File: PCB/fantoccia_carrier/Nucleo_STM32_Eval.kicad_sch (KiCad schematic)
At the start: 2 parts, among them J1 BU2450SM-JJ-GTR, U1 NUCLEO144-H743ZI

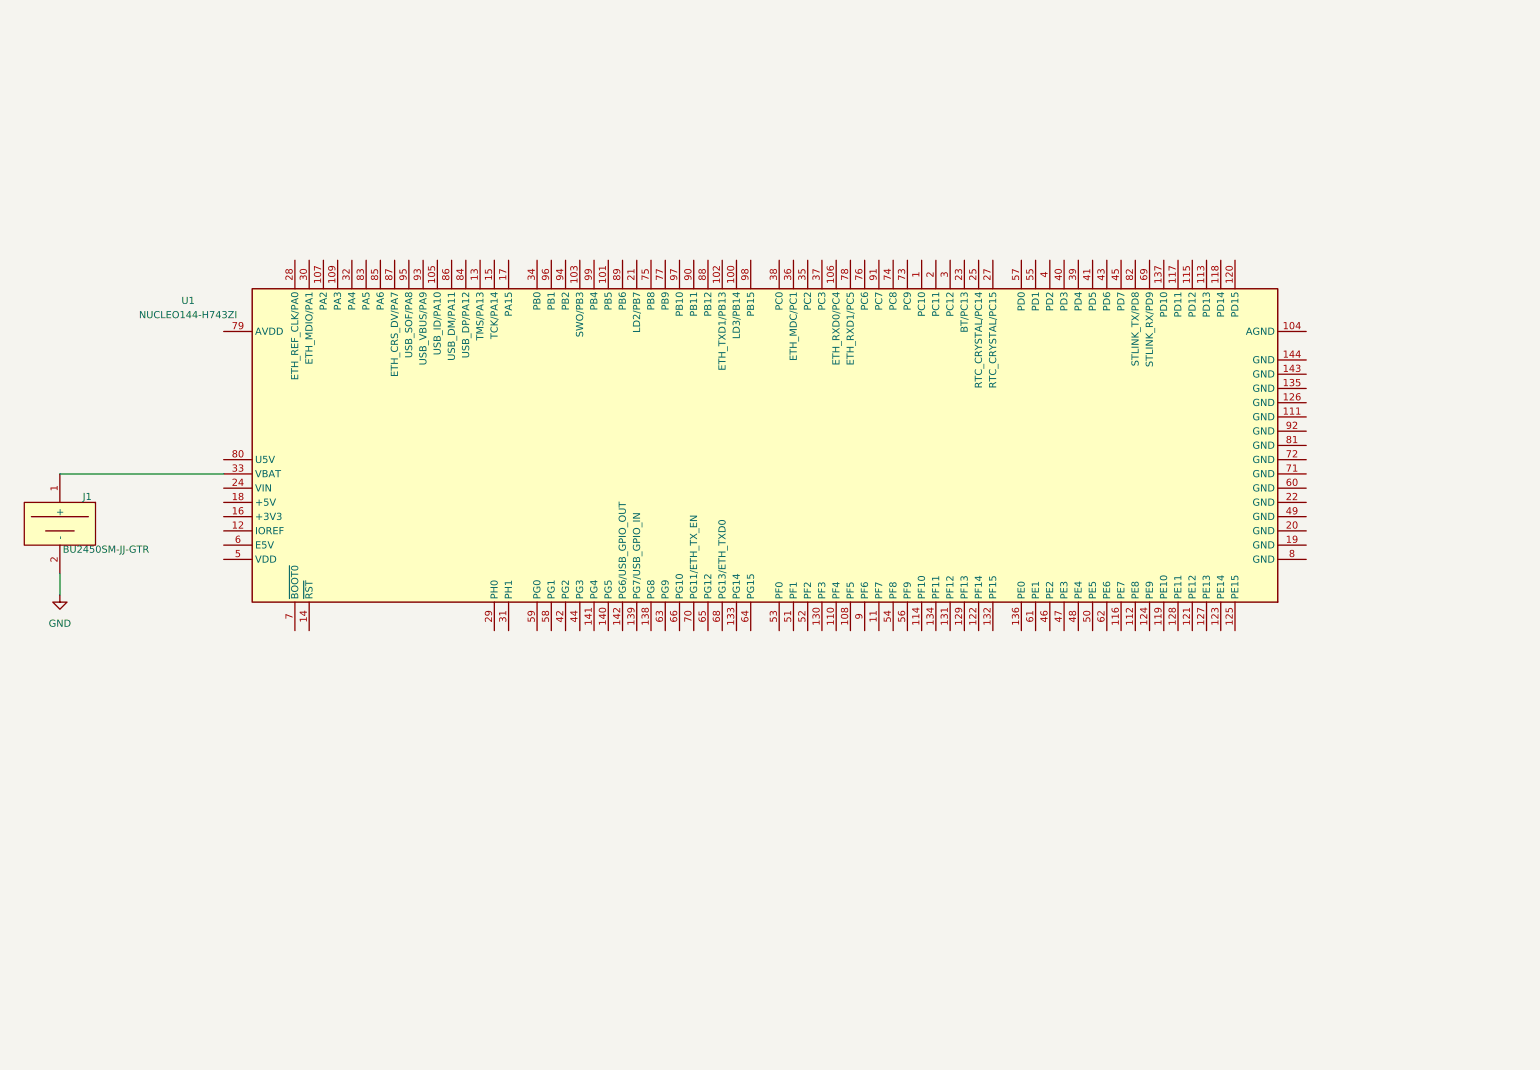
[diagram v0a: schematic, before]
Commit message: PCB Created
Schematic mostly finished, just need to figure out pinning and add more TVS protection. Created PCB might need to tweak footprint.
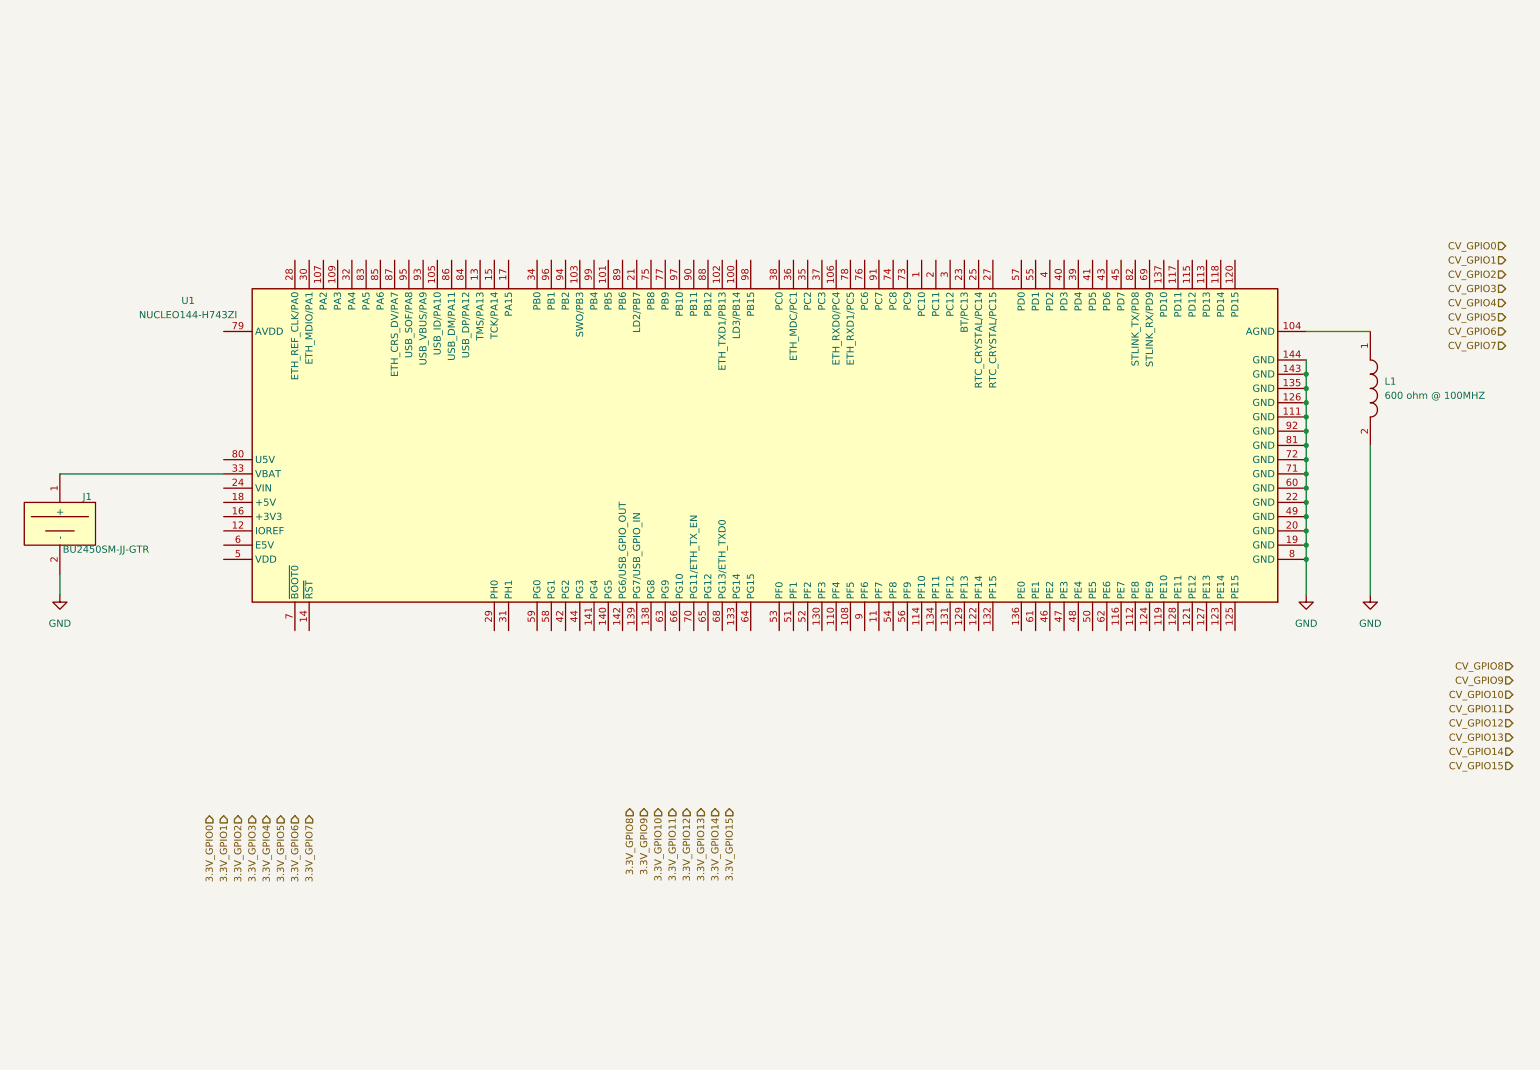
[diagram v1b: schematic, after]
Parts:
- added L1: HZ0805E601R-10, AVR-KiCAD-Lib-Inductors:HZ0805E601R-10, symbol AVR-KiCAD-Lib-Inductors:HZ0805E601R-10
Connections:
- net GND: now also U1.111 (GND), U1.126 (GND), U1.135 (GND), U1.143 (GND), U1.144 (GND), U1.19 (GND), U1.20 (GND), U1.22 (GND), U1.49 (GND), U1.60 (GND), U1.71 (GND), U1.72 (GND), U1.8 (GND), U1.81 (GND), U1.92 (GND), L1.2
- net at U1.104 (AGND): now also L1.1

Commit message: PCB progress and feature updates
Added another bank of 5V channels. PCB layout figured out, board shape defined. 3D model added to STM32 evaluation kit. Now just need to determine pinout and add protection circuitry to pins.
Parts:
- added D1, D2, D3, D4: LTST-C194TBKT, AVR-KiCAD-Lib-Diodes:LED0603, symbol AVR-KiCAD-Lib-Diodes:LTST-C194TBKT
- added R1, R2, R3, R4: RC0603FR-072K2L, AVR-KiCAD-Lib-Resistors:R0603, symbol AVR-KiCAD-Lib-Resistors:RC0603FR-072K2L
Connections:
- net GND: now also D1.2, D2.2, D3.2, D4.2
- new net: D4.1, R4.2
- new net: D1.1, R1.2
- new net: D3.1, R3.2
- new net: D2.1, R2.2

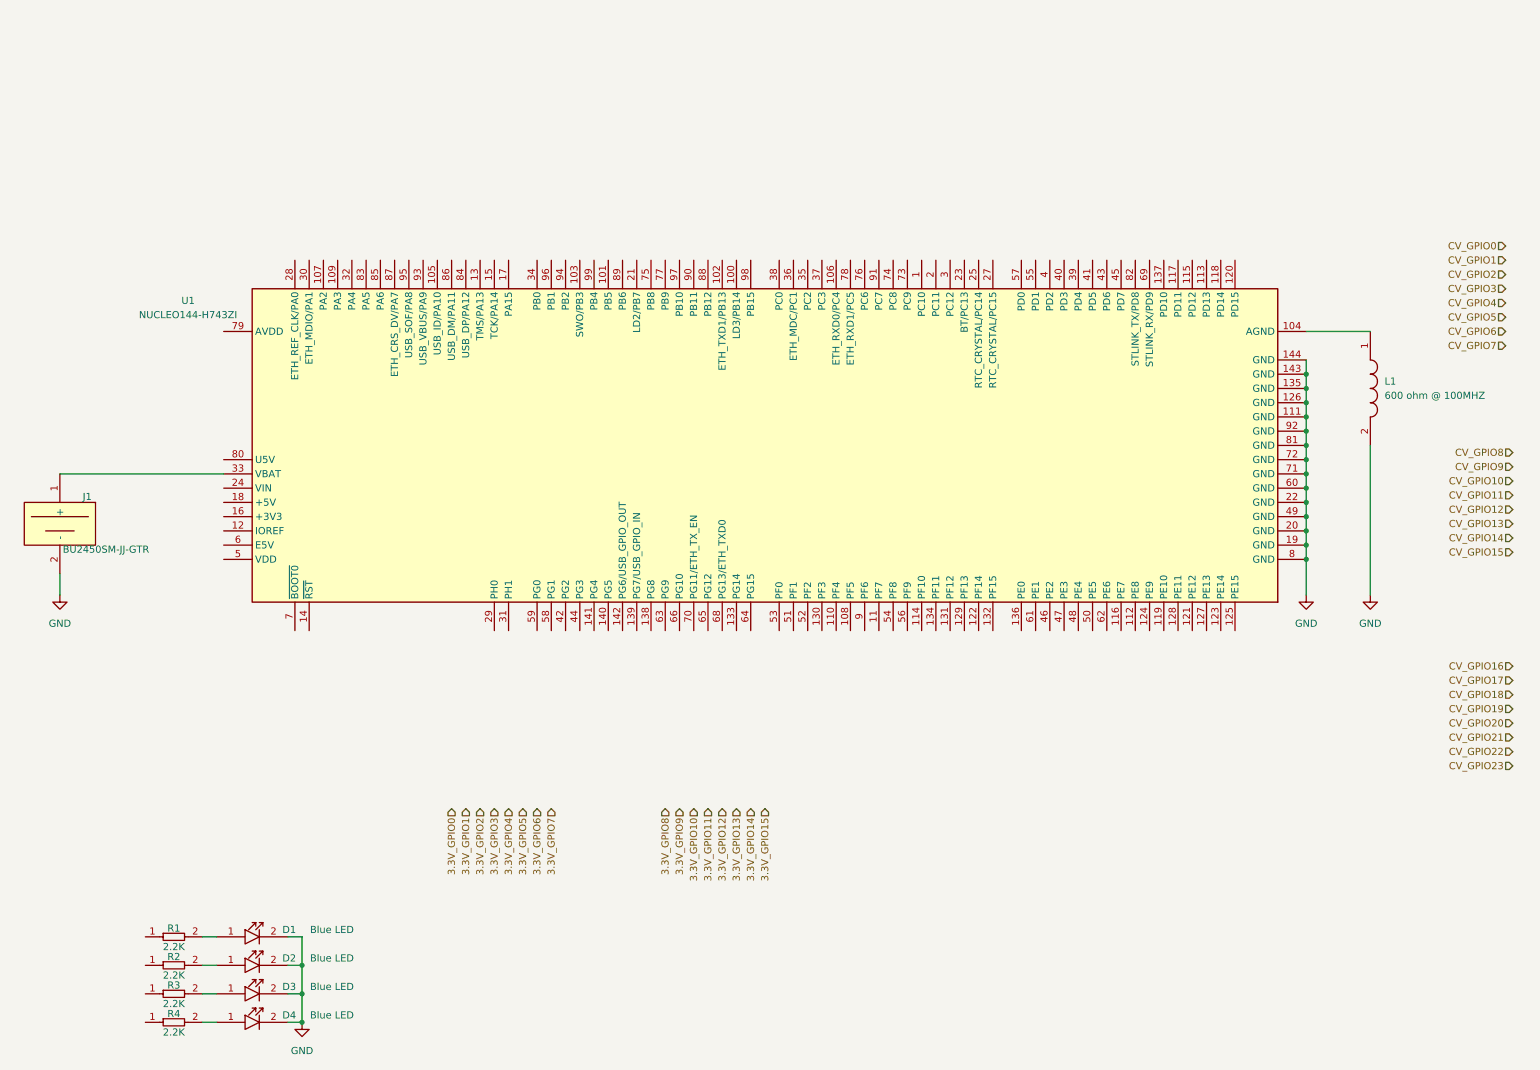
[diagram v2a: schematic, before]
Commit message: Design Rules
Created Design rules, added more IO connections, need to figure out pinning next.
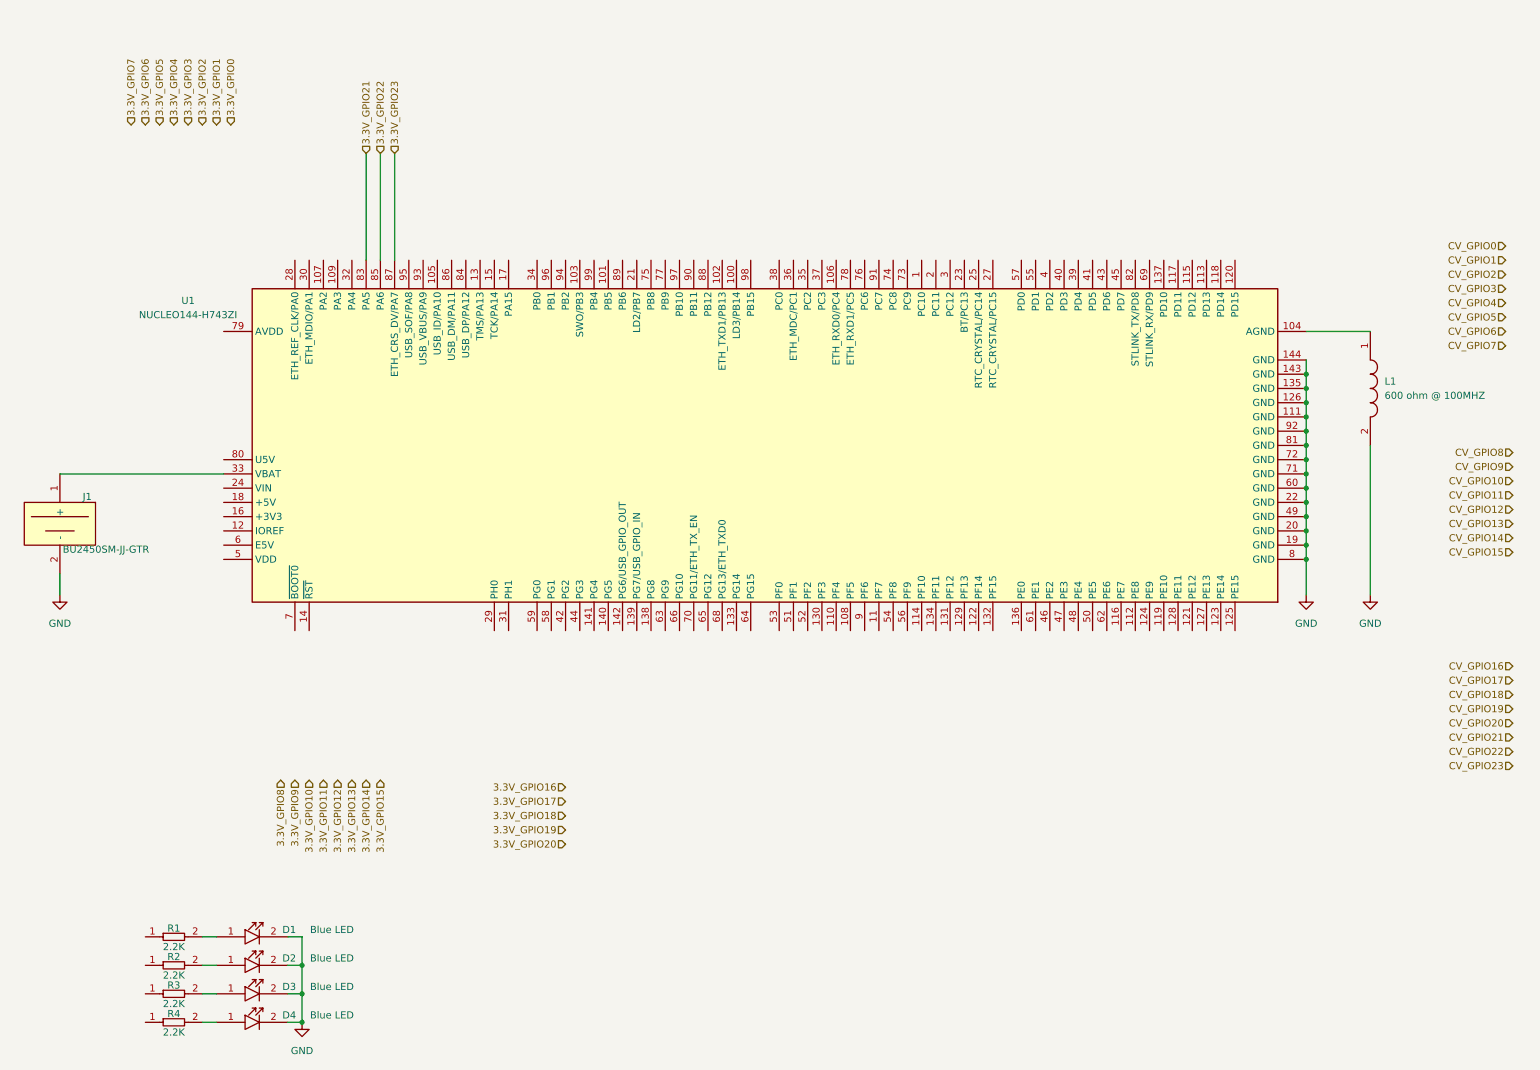
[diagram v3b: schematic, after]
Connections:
- net 3.3V_GPIO21: now reaches U1.83 (PA5)
- net 3.3V_GPIO22: now reaches U1.85 (PA6)
- net 3.3V_GPIO23: now reaches U1.87 (ETH_CRS_DV/PA7)
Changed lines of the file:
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@@
+	(wire
+		(pts
+			(xy 74.93 35.56) (xy 74.93 54.61)
+		)
+		(stroke
+			(width 0)
+			(type default)
+		)
+	)
 	(wire
 		(pts
@@
 	(wire
 		(pts
+			(xy 77.47 35.56) (xy 77.47 54.61)
+		)
+		(stroke
+			(width 0)
+			(type default)
+		)
+	)
+	(wire
+		(pts
+			(xy 80.01 35.56) (xy 80.01 54.61)
+		)
+		(stroke
+			(width 0)
+			(type default)
+		)
+	)
+	(wire
+		(pts
 			(xy 242.57 80.01) (xy 242.57 82.55)
 		)
@@
 	(hierarchical_label "3.3V_GPIO3"
 		(shape input)
-		(at 97.79 152.4 270)
-		(fields_autoplaced yes)
-		(effects
-			(font
-				(size 1.27 1.27)
-			)
-			(justify right)
+		(at 43.18 30.48 90)
+		(fields_autoplaced yes)
+		(effects
+			(font
+				(size 1.27 1.27)
+			)
+			(justify left)
+		)
+	)
+	(hierarchical_label "3.3V_GPIO23"
+		(shape input)
+		(at 80.01 35.56 90)
+		(fields_autoplaced yes)
+		(effects
+			(font
+				(size 1.27 1.27)
+			)
+			(justify left)
 		)
 	)
 	(hierarchical_label "3.3V_GPIO4"
 		(shape input)
-		(at 100.33 152.4 270)
-		(fields_autoplaced yes)
-		(effects
-			(font
-				(size 1.27 1.27)
-			)
-			(justify right)
+		(at 40.64 30.48 90)
+		(fields_autoplaced yes)
+		(effects
+			(font
+				(size 1.27 1.27)
+			)
+			(justify left)
 		)
 	)
@@
 	(hierarchical_label "3.3V_GPIO7"
 		(shape input)
-		(at 107.95 152.4 270)
-		(fields_autoplaced yes)
-		(effects
-			(font
-				(size 1.27 1.27)
-			)
-			(justify right)
+		(at 33.02 30.48 90)
+		(fields_autoplaced yes)
+		(effects
+			(font
+				(size 1.27 1.27)
+			)
+			(justify left)
 		)
 	)
 	(hierarchical_label "3.3V_GPIO2"
 		(shape input)
-		(at 95.25 152.4 270)
-		(fields_autoplaced yes)
-		(effects
-			(font
-				(size 1.27 1.27)
-			)
-			(justify right)
+		(at 45.72 30.48 90)
+		(fields_autoplaced yes)
+		(effects
+			(font
+				(size 1.27 1.27)
+			)
+			(justify left)
 		)
 	)
@@
 	(hierarchical_label "3.3V_GPIO1"
 		(shape input)
-		(at 92.71 152.4 270)
-		(fields_autoplaced yes)
-		(effects
-			(font
-				(size 1.27 1.27)
-			)
-			(justify right)
+		(at 48.26 30.48 90)
+		(fields_autoplaced yes)
+		(effects
+			(font
+				(size 1.27 1.27)
+			)
+			(justify left)
 		)
 	)
 	(hierarchical_label "3.3V_GPIO15"
 		(shape input)
-		(at 146.05 152.4 270)
+		(at 77.47 147.32 270)
 		(fields_autoplaced yes)
 		(effects
@@
 	(hierarchical_label "3.3V_GPIO9"
 		(shape input)
-		(at 130.81 152.4 270)
+		(at 62.23 147.32 270)
 		(fields_autoplaced yes)
 		(effects
@@
 	(hierarchical_label "3.3V_GPIO14"
 		(shape input)
-		(at 143.51 152.4 270)
+		(at 74.93 147.32 270)
 		(fields_autoplaced yes)
 		(effects
@@
 	(hierarchical_label "3.3V_GPIO10"
 		(shape input)
-		(at 133.35 152.4 270)
+		(at 64.77 147.32 270)
 		(fields_autoplaced yes)
 		(effects
@@
 	(hierarchical_label "3.3V_GPIO12"
 		(shape input)
-		(at 138.43 152.4 270)
+		(at 69.85 147.32 270)
 		(fields_autoplaced yes)
 		(effects
@@
 	(hierarchical_label "3.3V_GPIO6"
 		(shape input)
-		(at 105.41 152.4 270)
-		(fields_autoplaced yes)
-		(effects
-			(font
-				(size 1.27 1.27)
-			)
-			(justify right)
+		(at 35.56 30.48 90)
+		(fields_autoplaced yes)
+		(effects
+			(font
+				(size 1.27 1.27)
+			)
+			(justify left)
 		)
 	)
@@
 	(hierarchical_label "3.3V_GPIO0"
 		(shape input)
-		(at 90.17 152.4 270)
-		(fields_autoplaced yes)
-		(effects
-			(font
-				(size 1.27 1.27)
-			)
-			(justify right)
+		(at 50.8 30.48 90)
+		(fields_autoplaced yes)
+		(effects
+			(font
+				(size 1.27 1.27)
+			)
+			(justify left)
+		)
+	)
+	(hierarchical_label "3.3V_GPIO21"
+		(shape input)
+		(at 74.93 35.56 90)
+		(fields_autoplaced yes)
+		(effects
+			(font
+				(size 1.27 1.27)
+			)
+			(justify left)
 		)
 	)
@@
 	(hierarchical_label "3.3V_GPIO5"
 		(shape input)
-		(at 102.87 152.4 270)
-		(fields_autoplaced yes)
-		(effects
-			(font
-				(size 1.27 1.27)
-			)
-			(justify right)
+		(at 38.1 30.48 90)
+		(fields_autoplaced yes)
+		(effects
+			(font
+				(size 1.27 1.27)
+			)
+			(justify left)
 		)
 	)
@@
 	(hierarchical_label "3.3V_GPIO11"
 		(shape input)
-		(at 135.89 152.4 270)
+		(at 67.31 147.32 270)
 		(fields_autoplaced yes)
 		(effects
@@
 		)
 	)
+	(hierarchical_label "3.3V_GPIO22"
+		(shape input)
+		(at 77.47 35.56 90)
+		(fields_autoplaced yes)
+		(effects
+			(font
+				(size 1.27 1.27)
+			)
+			(justify left)
+		)
+	)
+	(hierarchical_label "3.3V_GPIO16"
+		(shape input)
+		(at 110.49 148.59 180)
+		(fields_autoplaced yes)
+		(effects
+			(font
+				(size 1.27 1.27)
+			)
+			(justify right)
+		)
+	)
 	(hierarchical_label "CV_GPIO12"
 		(shape input)
@@
 	(hierarchical_label "3.3V_GPIO8"
 		(shape input)
-		(at 128.27 152.4 270)
+		(at 59.69 147.32 270)
+		(fields_autoplaced yes)
+		(effects
+			(font
+				(size 1.27 1.27)
+			)
+			(justify right)
+		)
+	)
+	(hierarchical_label "3.3V_GPIO19"
+		(shape input)
+		(at 110.49 156.21 180)
 		(fields_autoplaced yes)
 		(effects
@@
 		)
 	)
+	(hierarchical_label "3.3V_GPIO17"
+		(shape input)
+		(at 110.49 151.13 180)
+		(fields_autoplaced yes)
+		(effects
+			(font
+				(size 1.27 1.27)
+			)
+			(justify right)
+		)
+	)
 	(hierarchical_label "CV_GPIO0"
 		(shape input)
@@
 		)
 	)
+	(hierarchical_label "3.3V_GPIO18"
+		(shape input)
+		(at 110.49 153.67 180)
+		(fields_autoplaced yes)
+		(effects
+			(font
+				(size 1.27 1.27)
+			)
+			(justify right)
+		)
+	)
 	(hierarchical_label "CV_GPIO13"
 		(shape input)
@@
 	(hierarchical_label "3.3V_GPIO13"
 		(shape input)
-		(at 140.97 152.4 270)
+		(at 72.39 147.32 270)
 		(fields_autoplaced yes)
 		(effects
@@
 		(fields_autoplaced yes)
 		(effects
+			(font
+				(size 1.27 1.27)
+			)
+			(justify right)
+		)
+	)
+	(hierarchical_label "3.3V_GPIO20"
+		(shape input)
+		(at 110.49 158.75 180)
+		(fields_autoplaced yes)
+		(effects
